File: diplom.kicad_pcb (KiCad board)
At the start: 2 copper layers, 110 x 110 mm, 128 parts, among them J1 USB_B, J2 Barrel_Jack, J3 USB_B, J4 Screw_Terminal_01x03, J5 Screw_Terminal_01x04, J6 Screw_Terminal_01x04, J7 Screw_Terminal_01x04, J8 Screw_Terminal_01x02, Q1 S8050, SW1 SW_Push, SW2 SW_SPST, SW3 SW_SPDT, SW4 SW_SPDT, SW5 SW_Push, SW6 SW_Push, SW7 SW_Push, SW8 SW_Push, U1 LD3985M33R, U10 L298, U11 LS7366R, U12 LS7366R, U2 TPS54620, U3 STM32F103_STLINK, U4 CP2102, U5 TPS76833, U6 STM32F446, U7 STM32F103_DC, U8 TCA9517, U9 PCF8574, Y1 8MHz, Y2 8MHz, Y3 20MHz, Y4 20MHz

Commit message: PCB routing started. Quartz footprint changed
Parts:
- RV1: moved to F.Cu
- Y1, Y2, Y3, Y4: footprint Crystals:Crystal_SMD_HC49-SD_HandSoldering -> Crystals:Crystal_SMD_EuroQuartz_MQ2-2pin_7.0x5.0mm_HandSoldering
- moved SW2 5.50 mm to (58.5, 118.5), turned to 90 degrees
- moved C13 3.61 mm to (75.0, 130.5)
- moved U2 3.54 mm to (86.5, 130.0)
- moved J2 3.50 mm to (65.5, 129.5)
- moved C3 3.35 mm to (87.0, 135.5), turned to 0 degrees
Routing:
- net GND: track 0.00 -> 561.8 mm, vias 0 -> 24
- net +5V: track 0.00 -> 217.2 mm, vias 0 -> 9
- net +3V3: track 0.00 -> 183.3 mm, vias 0 -> 6
- net +12V: track 0.00 -> 68.4 mm, vias 0 -> 2
- net Net-(D7-Pad2): track 0.00 -> 65.4 mm, vias 0 -> 1
- net Net-(DS1-Pad16): track 0.00 -> 61.8 mm, vias 0 -> 1
- net +3.3VA: track 0.00 -> 53.3 mm
- net Net-(D5-Pad2): track 0.00 -> 45.2 mm, vias 0 -> 3
- net Net-(DS1-Pad3): track 0.00 -> 34.6 mm, vias 0 -> 1
- net Net-(DS1-Pad5): track 0.00 -> 33.1 mm, vias 0 -> 2
- net Net-(DS1-Pad6): track 0.00 -> 32.3 mm, vias 0 -> 2
- net Net-(DS1-Pad14): track 0.00 -> 27.8 mm, vias 0 -> 1
- net Net-(R24-Pad1): track 0.00 -> 23.3 mm
- net Net-(DS1-Pad13): track 0.00 -> 21.8 mm, vias 0 -> 1
- net Net-(D1-Pad2): track 0.00 -> 20.7 mm
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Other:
- net class Default: trace_width 0.25 -> 0.4; via_dia 0.6 -> 0.8; via_drill 0.4 -> 0.6
- rule trace_min: 0.2 -> 0.4
- rule via_min_drill: 0.3 -> 0.6
- rule via_min_size: 0.4 -> 0.8

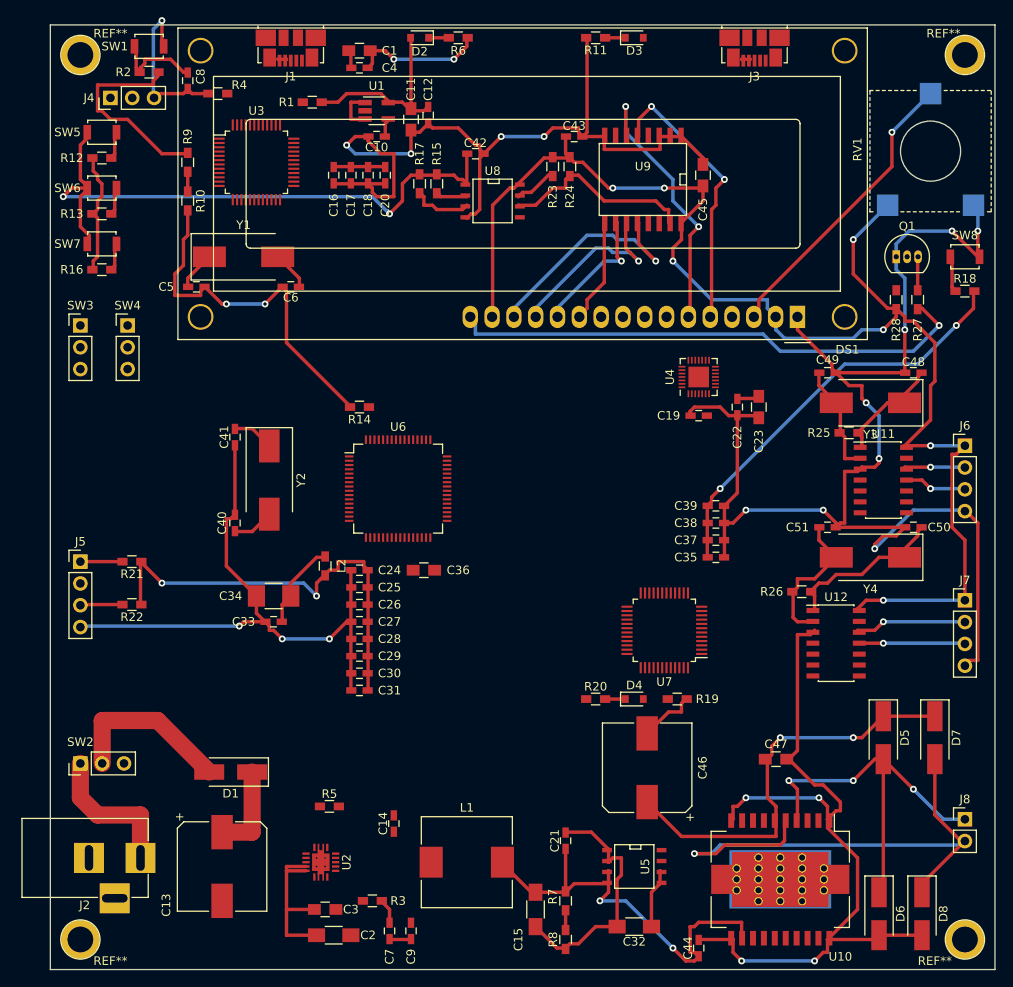
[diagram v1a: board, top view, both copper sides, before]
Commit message: PCB redrawing with correct net
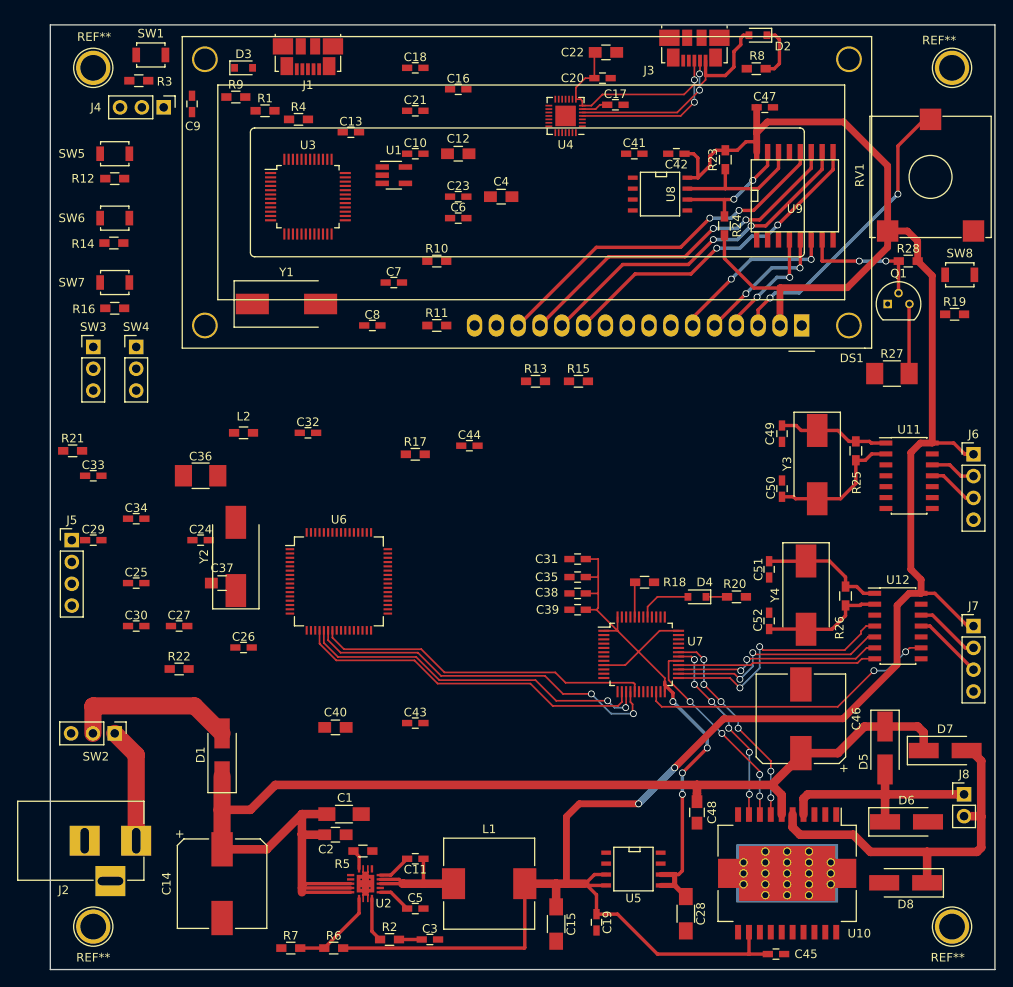
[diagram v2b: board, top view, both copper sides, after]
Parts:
- removed the REF** at (161.5, 36.0)
- removed the REF** at (161.5, 139.0)
- removed the REF** at (58.5, 36.0)
- removed the REF** at (58.5, 139.0)
- added C52: 15p, Capacitors_SMD:C_0603_HandSoldering, F.Cu at (138.7, 101.9)
- added REF**: 1pin, Connectors:1pin, F.Cu at (60.0, 37.5)
- added REF**: 1pin, Connectors:1pin, F.Cu at (160.0, 37.5)
- added REF**: 1pin, Connectors:1pin, F.Cu at (160.0, 137.5)
- added REF**: 1pin, Connectors:1pin, F.Cu at (60.0, 137.5)
- C1: value 1u -> 10u; footprint Capacitors_SMD:C_0805_HandSoldering -> Capacitors_SMD:C_1206_HandSoldering
- C11: value 1u -> 0.1u; footprint Capacitors_SMD:C_0805_HandSoldering -> Capacitors_SMD:C_0603_HandSoldering
- C12, C37, C4: value 100n -> 1u; footprint Capacitors_SMD:C_0603_HandSoldering -> Capacitors_SMD:C_0805_HandSoldering
- C13: value 330u -> 100n; footprint Capacitors_SMD:CP_Elec_10x10 -> Capacitors_SMD:C_0603_HandSoldering
- C14: value 0.1u -> 330u; footprint Capacitors_SMD:C_0603_HandSoldering -> Capacitors_SMD:CP_Elec_10x10
- C17, C20: value 100n -> 0.1u
- C19: value 0.1u -> 100n
- C2: value 10u -> 4.7u; footprint Capacitors_SMD:C_1206_HandSoldering -> Capacitors_SMD:C_0805_HandSoldering
- C22: value 0.1u -> 1u; footprint Capacitors_SMD:C_0603_HandSoldering -> Capacitors_SMD:C_0805_HandSoldering
- C23: value 1u -> 100n; footprint Capacitors_SMD:C_0805_HandSoldering -> Capacitors_SMD:C_0603_HandSoldering
- C28: value 100n -> 10u; footprint Capacitors_SMD:C_0603_HandSoldering -> Capacitors_SMD:C_1206_HandSoldering
- C3: value 4.7u -> 8200p; footprint Capacitors_SMD:C_0805_HandSoldering -> Capacitors_SMD:C_0603_HandSoldering
- C32: value 10u -> 100n; footprint Capacitors_SMD:C_1206_HandSoldering -> Capacitors_SMD:C_0603_HandSoldering
- C34: value 1u -> 100n; footprint Capacitors_SMD:C_1210_HandSoldering -> Capacitors_SMD:C_0603_HandSoldering
- C36: value 4.7u -> 1u; footprint Capacitors_SMD:C_0805_HandSoldering -> Capacitors_SMD:C_1210_HandSoldering
- C40: value 20p -> 4.7u; footprint Capacitors_SMD:C_0603_HandSoldering -> Capacitors_SMD:C_0805_HandSoldering
- C41, C6: value 20p -> 100n
- C43, C8: value 100n -> 20p
- C44: value 0.1u -> 20p
- C45, C47: footprint Capacitors_SMD:C_0805_HandSoldering -> Capacitors_SMD:C_0603_HandSoldering
- C48: value 15p -> 0.1u; footprint Capacitors_SMD:C_0603_HandSoldering -> Capacitors_SMD:C_0805_HandSoldering
- C5: value 20p -> 0.01u
- C7: value 8200p -> 20p
- C9: value 0.01u -> 100n
- Q1: footprint TO_SOT_Packages_THT:TO-92_Inline_Narrow_Oval -> TO_SOT_Packages_THT:TO-92_Molded_Narrow
- R11: value 2K2 -> 4K7
- R13, R8: value 10K -> 4K7
- R14, R19: value 100K -> 10K
- R17: value 4K7 -> 100K
- R18: value 10K -> 100K
- R2: value 100K -> 1K69
- R21: value 470 -> 2K2
- R22: value 2K2 -> 470
- R27: footprint Resistors_SMD:R_0603_HandSoldering -> Resistors_SMD:R_1210_HandSoldering
- R3: value 1K69 -> 100K
- R6: value 2K2 -> 52K5
- R7: value 52K5 -> 10K
- R9: value 4K7 -> 2K2
- RV1: value 10K -> POT; footprint Potentiometers:Potentiometer_Trimmer_ACP_CA14VSMD_Horizontal_Px13.0mm_Py10.0mm_MountLS -> Potentiometers:Potentiometer_Trimmer_ACP_CA14VSMD_Horizontal_Px13.0mm_Py10.0mm
- moved R6 107.0 mm to (88.0, 140.0)
- moved R2 104.8 mm to (94.5, 139.0)
- moved R8 103.8 mm to (137.2, 37.6), turned to 0 degrees
- moved C9 99.6 mm to (71.5, 41.7)
- moved R3 99.3 mm to (65.3, 39.0)
- moved C45 91.1 mm to (139.5, 140.7), turned to 0 degrees
- moved C1 88.9 mm to (89.2, 124.4)
- moved C13 86.8 mm to (90.0, 45.0), turned to 0 degrees
- moved C21 86.8 mm to (97.5, 42.5), turned to 0 degrees
- moved C11 86.1 mm to (97.5, 129.6), turned to 180 degrees
- moved C5 76.8 mm to (97.5, 135.4)
- moved C47 75.9 mm to (138.2, 42.1)
- moved C7 75.5 mm to (95.0, 62.5), turned to 0 degrees
- moved C43 70.8 mm to (97.5, 113.8)
- moved C32 68.9 mm to (85.0, 80.0), turned to 0 degrees
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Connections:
- net MISO renamed /MISO
- net MOSI renamed /MOSI
- net Net-(J1-Pad2) renamed /DN
- net SCK renamed /SCK
- net SS renamed /SS
- C1 pad 1: Net-(C1-Pad1) -> +12V
- C11 pad 1: +3.3VA -> Net-(C11-Pad1)
- C11 pad 2: GND -> Net-(C11-Pad2)
- C13 pad 1: Net-(C13-Pad1) -> +3.3VA
- C14 pad 1: Net-(C14-Pad1) -> +12V
- C14 pad 2: Net-(C14-Pad2) -> GND
- C17 pad 1: +3.3VA -> Net-(C17-Pad1)
- C19 pad 1: Net-(C19-Pad1) -> +5V
- C20 pad 1: +3.3VA -> Net-(C20-Pad1)
- C21 pad 1: +5V -> +3.3VA
- C22 pad 1: Net-(C22-Pad1) -> Net-(C20-Pad1)
- C23 pad 1: Net-(C22-Pad1) -> +3.3VA
- C3 pad 1: +12V -> Net-(C3-Pad1)
- C32 pad 1: +3V3 -> Net-(C32-Pad1)
- C33 pad 1: Net-(C33-Pad1) -> +3V3
- C34 pad 1: Net-(C33-Pad1) -> +3V3
- C36 pad 1: Net-(C36-Pad1) -> Net-(C32-Pad1)
- C4 pad 1: Net-(C1-Pad1) -> VBUS
- C40 pad 1: GND -> Net-(C40-Pad1)
- C40 pad 2: Net-(C40-Pad2) -> GND
- C41 pad 1: GND -> +3V3
- C41 pad 2: Net-(C41-Pad2) -> GND
- C42 pad 1: +3V3 -> +5V
- C43 pad 1: +5V -> GND
- C43 pad 2: GND -> Net-(C43-Pad2)
- C44 pad 1: +5V -> GND
- C44 pad 2: GND -> Net-(C44-Pad2)
- C47 pad 1: +12V -> +5V
- C48 pad 1: GND -> +12V
- C48 pad 2: Net-(C48-Pad2) -> GND
- C6 pad 1: Net-(C6-Pad1) -> VBUS
- C7 pad 2: Net-(C7-Pad2) -> GND
- C9 pad 2: Net-(C7-Pad2) -> GND
- D1 pad 1: Net-(C13-Pad1) -> +12V
- D2 pad 2: +3.3VA -> Net-(C20-Pad1)
- D3 pad 2: Net-(D3-Pad2) -> +3.3VA
- J1 pad 1: Net-(C1-Pad1) -> VBUS
- J1 pad 3: Net-(J1-Pad3) -> /DP
- J3 pad 1: Net-(D3-Pad2) -> Net-(C20-Pad1)
- L1 pad 1: Net-(L1-Pad1) -> Net-(C11-Pad1)
- L2 pad 1: Net-(C33-Pad1) -> Net-(C32-Pad1)
- R1 pad 1: Net-(J1-Pad3) -> +3.3VA
- R1 pad 2: +3.3VA -> /DP
- R10 pad 1: GND -> Net-(R10-Pad1)
- R10 pad 2: Net-(R10-Pad2) -> +3.3VA
- R11 pad 1: Net-(D3-Pad1) -> GND
- R11 pad 2: GND -> Net-(R10-Pad1)
- R13 pad 1: GND -> /DISP_SCL
- R13 pad 2: /BTN2 -> +3V3
- R14 pad 1: Net-(R14-Pad1) -> GND
- R14 pad 2: GND -> /BTN2
- R15 pad 1: /DISP_SCL -> /DISP_SDA
- R17 pad 1: /DISP_SDA -> GND
- R17 pad 2: +3V3 -> Net-(R17-Pad2)
- R18 pad 1: /N_RST -> GND
- R18 pad 2: +3V3 -> Net-(R18-Pad2)
- R19 pad 1: Net-(R19-Pad1) -> /N_RST
- R19 pad 2: GND -> +3V3
- R2 pad 1: Net-(C8-Pad1) -> Net-(R2-Pad1)
- R2 pad 2: +3.3VA -> Net-(C3-Pad1)
- R21 pad 1: +3V3 -> Net-(J5-Pad3)
- R21 pad 2: Net-(J5-Pad1) -> +3V3
- R22 pad 1: +3V3 -> Net-(J5-Pad1)
- R22 pad 2: Net-(J5-Pad3) -> +3V3
- R25 pad 1: Net-(C49-Pad2) -> Net-(C50-Pad2)
- R25 pad 2: Net-(C48-Pad2) -> Net-(C49-Pad2)
- R26 pad 1: Net-(C51-Pad2) -> Net-(C52-Pad2)
- R26 pad 2: Net-(C50-Pad2) -> Net-(C51-Pad2)
- R3 pad 1: Net-(R3-Pad1) -> +3.3VA
- R3 pad 2: Net-(C7-Pad1) -> Net-(C9-Pad1)
- R4 pad 1: GND -> Net-(R4-Pad1)
- R4 pad 2: Net-(R4-Pad2) -> GND
- R6 pad 1: Net-(D2-Pad1) -> Net-(R6-Pad1)
- R6 pad 2: GND -> +5V
- R7 pad 1: Net-(R7-Pad1) -> GND
- R7 pad 2: +5V -> Net-(R6-Pad1)
- R8 pad 2: Net-(R7-Pad1) -> Net-(D2-Pad1)
- R9 pad 1: Net-(R10-Pad2) -> GND
- R9 pad 2: +3.3VA -> Net-(D3-Pad1)
- SW1 pad 1: Net-(C8-Pad1) -> Net-(C9-Pad1)
- U1 pad 1: Net-(C1-Pad1) -> VBUS
- U1 pad 3: Net-(C1-Pad1) -> VBUS
- U11 pad 1: Net-(C48-Pad2) -> Net-(C49-Pad2)
- U11 pad 2: Net-(C49-Pad2) -> Net-(C50-Pad2)
- U12 pad 1: Net-(C50-Pad2) -> Net-(C51-Pad2)
- U12 pad 2: Net-(C51-Pad2) -> Net-(C52-Pad2)
- U2 pad 11: Net-(L1-Pad1) -> Net-(C11-Pad1)
- U2 pad 12: Net-(C14-Pad1) -> Net-(C11-Pad1)
- U2 pad 13: Net-(C14-Pad2) -> Net-(C11-Pad2)
- U2 pad 7: Net-(R7-Pad1) -> Net-(R6-Pad1)
- U2 pad 8: Net-(R3-Pad1) -> Net-(R2-Pad1)
- U2 pad 9: Net-(C9-Pad1) -> Net-(C5-Pad1)
- U3 pad 10: Net-(R10-Pad2) -> Net-(R10-Pad1)
- U3 pad 33: Net-(J1-Pad3) -> /DP
- U3 pad 44: Net-(R4-Pad2) -> Net-(R4-Pad1)
- U3 pad 5: Net-(C5-Pad1) -> Net-(C7-Pad1)
- U3 pad 6: Net-(C6-Pad1) -> Net-(C8-Pad1)
- U3 pad 7: Net-(C8-Pad1) -> Net-(C9-Pad1)
- U4 pad 6: Net-(C19-Pad1) -> Net-(C17-Pad1)
- U4 pad 7: Net-(C22-Pad1) -> Net-(C20-Pad1)
- U4 pad 8: Net-(D3-Pad2) -> Net-(C20-Pad1)
- U6 pad 13: Net-(C33-Pad1) -> Net-(C32-Pad1)
- U6 pad 30: Net-(C36-Pad1) -> Net-(C40-Pad1)
- U6 pad 5: Net-(C41-Pad2) -> Net-(C43-Pad2)
- U6 pad 6: Net-(C40-Pad2) -> Net-(C44-Pad2)
- U6 pad 60: Net-(R14-Pad1) -> Net-(R17-Pad2)
- U7 pad 44: Net-(R19-Pad1) -> Net-(R18-Pad2)
- Y1 pad 1: Net-(C5-Pad1) -> Net-(C7-Pad1)
- Y1 pad 2: Net-(C6-Pad1) -> Net-(C8-Pad1)
- Y2 pad 1: Net-(C41-Pad2) -> Net-(C43-Pad2)
- Y2 pad 2: Net-(C40-Pad2) -> Net-(C44-Pad2)
- Y3 pad 1: Net-(C48-Pad2) -> Net-(C49-Pad2)
- Y3 pad 2: Net-(C49-Pad2) -> Net-(C50-Pad2)
- Y4 pad 1: Net-(C50-Pad2) -> Net-(C51-Pad2)
- Y4 pad 2: Net-(C51-Pad2) -> Net-(C52-Pad2)
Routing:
- net GND: track 561.8 -> 0.00 mm, vias 24 -> 0
- net +3V3: track 183.3 -> 70.7 mm, vias 6 -> 4
- net +12V: track 68.4 -> 145.6 mm, vias 2 -> 0
- net Net-(DS1-Pad16): track 61.8 -> 0.00 mm, vias 1 -> 0
- net +5V: track 217.2 -> 273.8 mm, vias 9 -> 2
- net +3.3VA: track 53.3 -> 0.00 mm
- net /MISO: track 0.00 -> 42.9 mm, vias 0 -> 2
- net /SCK: track 0.00 -> 41.6 mm, vias 0 -> 2
- net /SS: track 0.00 -> 41.1 mm
- net /MOSI: track 0.00 -> 39.2 mm
- net /OE2_FLAG: track 0.00 -> 35.1 mm, vias 0 -> 2
- net Net-(C20-Pad1): track 0.00 -> 34.7 mm
- net /OE2_SS: track 0.00 -> 28.3 mm, vias 0 -> 2
- net /OE2_SCK: track 0.00 -> 26.3 mm, vias 0 -> 2
- net Net-(DS1-Pad11): track 12.4 -> 38.6 mm, vias 0 -> 2
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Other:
- net class Default: clearance 0.2 -> 0.05
- rule trace_clearance: 0.2 -> 0.05
- rule trace_min: 0.4 -> 0.2

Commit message: PCB routed
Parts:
- added REF**: 1pin, Connectors:1pin, F.Cu at (91.7, 132.5)
- moved R19 65.3 mm to (107.0, 104.0), turned to 270 degrees
- moved SW8 65.0 mm to (107.0, 98.0), turned to 90 degrees
- moved C41 36.7 mm to (99.0, 75.3), turned to 90 degrees
- moved C44 36.7 mm to (71.0, 98.0), turned to 270 degrees
- moved C42 36.2 mm to (110.0, 79.0), turned to 270 degrees
- moved U8 35.8 mm to (103.5, 80.0)
- moved C43 34.3 mm to (71.0, 92.0), turned to 90 degrees
- moved C7 28.0 mm to (70.5, 49.0), turned to 270 degrees
- moved C30 26.9 mm to (84.5, 84.0)
- moved C8 25.3 mm to (70.5, 55.0), turned to 90 degrees
- moved R11 25.0 mm to (76.0, 60.5)
- moved C32 24.9 mm to (79.3, 104.2)
- moved C36 22.5 mm to (77.9, 106.8)
- moved L2 22.4 mm to (79.5, 102.3)
- moved C27 22.3 mm to (84.5, 85.5)
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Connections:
- DS1 pad : (no net) -> GND
- REF** pad 1: (no net) -> GND (x4)
- U10 pad 21: (no net) -> GND
- U2 pad : (no net) -> GND
- U4 pad 29: (no net) -> GND
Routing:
- net +3V3: track 70.7 -> 405.6 mm, vias 4 -> 10
- net GND: track 0.00 -> 206.4 mm, vias 0 -> 80
- net +3.3VA: track 0.00 -> 109.0 mm, vias 0 -> 2
- net /SWD2_IO: track 0.00 -> 95.9 mm, vias 0 -> 4
- net /SWD2_CLK: track 0.00 -> 89.0 mm, vias 0 -> 4
- net /BTN1: track 0.00 -> 83.9 mm, vias 0 -> 6
- net /OE1_FLAG: track 0.00 -> 79.7 mm, vias 0 -> 4
- net /BTN2: track 0.00 -> 76.1 mm, vias 0 -> 6
- net /BTN3: track 0.00 -> 70.8 mm, vias 0 -> 6
- net /OE1_MOSI: track 0.00 -> 69.0 mm, vias 0 -> 2
- net /OE1_SS: track 0.00 -> 68.1 mm, vias 0 -> 2
- net /OE1_MISO: track 0.00 -> 67.6 mm, vias 0 -> 2
- net /OE1_SCK: track 0.00 -> 67.2 mm, vias 0 -> 2
- net /STM_TX: track 0.00 -> 64.0 mm, vias 0 -> 2
- net /STM_RX: track 0.00 -> 63.5 mm
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- added copper zone on B.Cu, net GND
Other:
- rule via_min_drill: 0.6 -> 0.4
- rule via_min_size: 0.8 -> 0.6
